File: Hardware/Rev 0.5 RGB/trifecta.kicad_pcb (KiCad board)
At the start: 2 copper layers, 361 x 120.8 mm, 286 parts, among them J1 USB2_C_Receptacle, J2 ISP Header, SW1 RESET, SW2 Rotary_Encoder_Switch, SW3 Rotary_Encoder_Switch, SW4 Rotary_Encoder_Switch, U1 ATmega32U4-AU, U2 SRV05-4, Y1 16MHz

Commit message: 8/8
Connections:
- J2 pad 5: RESET -> Net-(J2-Pad5)
- R1 pad 2: Net-(R1-Pad2) -> Net-(J2-Pad5)
- SW1 pad 2: Net-(R1-Pad2) -> Net-(J2-Pad5)
- U1 pad 13: Net-(R1-Pad2) -> Net-(J2-Pad5)
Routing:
- net Net-(R1-Pad2): track 38.4 -> 0.00 mm, vias 2 -> 0
- net Net-(J2-Pad5): track 0.00 -> 38.4 mm, vias 0 -> 2

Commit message: 8/8
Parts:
- J2: moved to B.Cu
- moved J2 3.52 mm to (157.5, -1.98), turned to 180 degrees
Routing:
- net row3: track 406.2 -> 458.6 mm, vias 7 -> 9
- net Net-(J2-Pad5): track 38.4 -> 90.5 mm, vias 2 -> 4
- net +5V: track 2351.0 -> 2382.4 mm, vias 90 -> 92
- net 0col: track 467.1 -> 491.4 mm
- net GND: track 2423.3 -> 2438.5 mm, vias 105 -> 107
- net col5: track 334.3 -> 349.4 mm, vias 1 -> 2
- added copper zone on B.Cu, net (none)
- added copper zone on F.Cu, net (none)

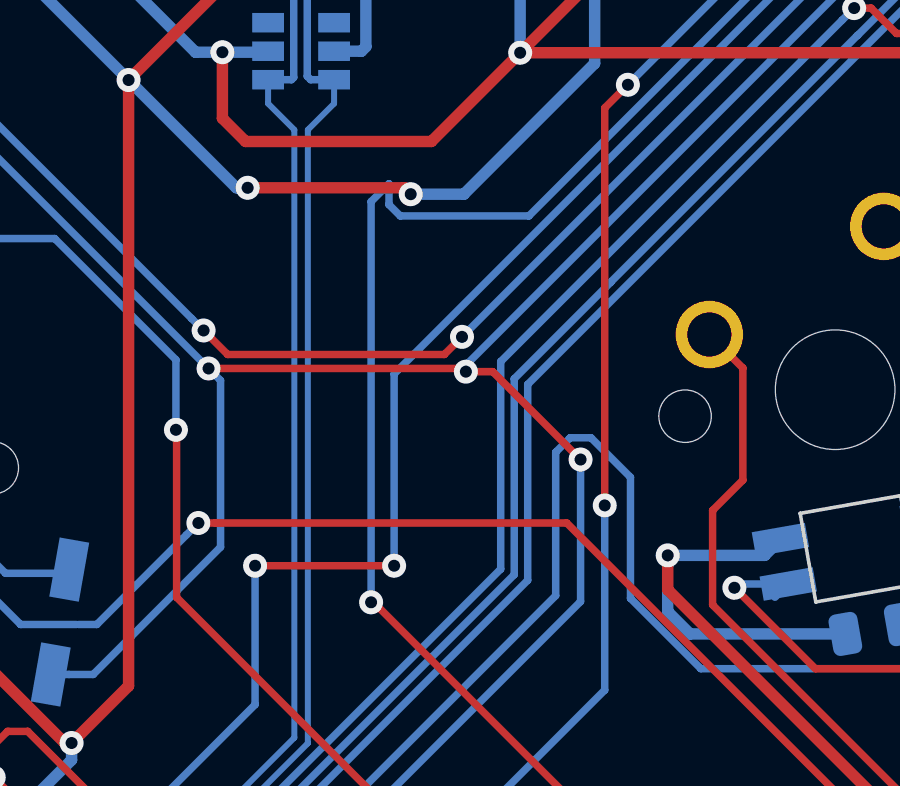
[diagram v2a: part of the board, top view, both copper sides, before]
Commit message: Clean up silkscreens, regenerate gerbers
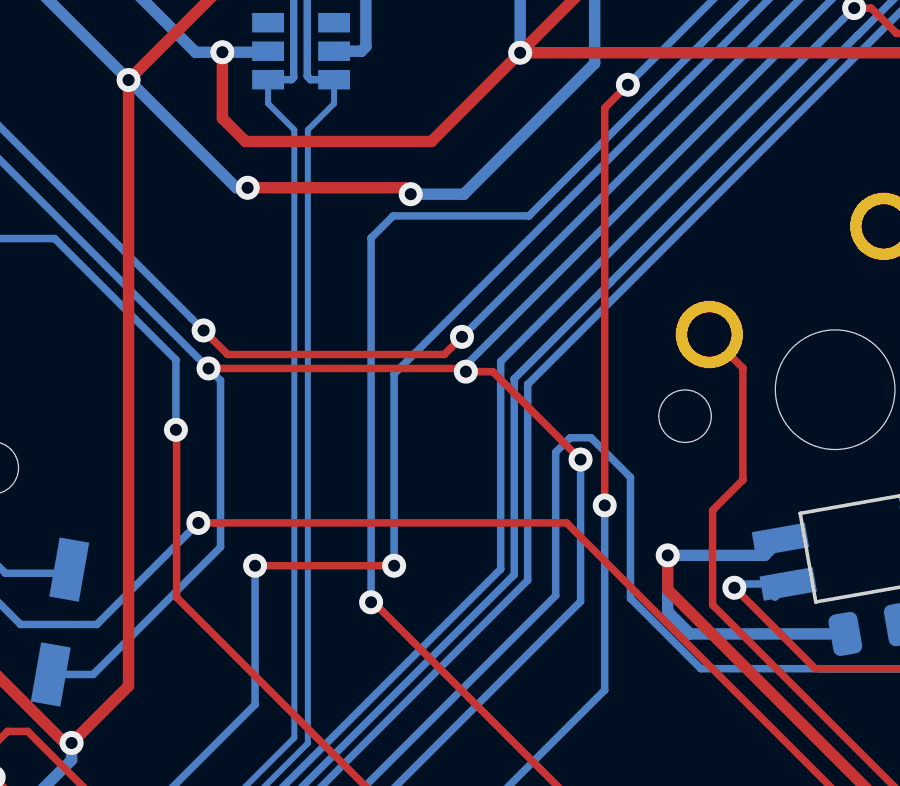
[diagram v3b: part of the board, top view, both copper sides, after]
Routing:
- net row3: track 458.6 -> 456.6 mm
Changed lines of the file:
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@@
-(kicad_pcb (version 20171130) (host pcbnew "(5.1.6)-1")
+(kicad_pcb (version 20171130) (host pcbnew "(5.1.4)-1")
   (general
     (thickness 1.6)
     (drawings 941)
-    (tracks 4406)
+    (tracks 4404)
     (zones 0)
     (modules 286)
@@
   (segment (start 152.25268 35.24504) (end 144.0688 27.06116) (width 0.25) (layer F.Cu) (net 10))
   (segment (start 144.0688 27.06116) (end 143.98244 27.06116) (width 0.25) (layer F.Cu) (net 10))
+  (segment (start 158.02356 0.5588) (end 157.46476 0.5588) (width 0.25) (layer B.Cu) (net 10))
+  (segment (start 143.98244 14.91756) (end 144.718079 14.181921) (width 0.25) (layer B.Cu) (net 10))
+  (segment (start 143.98244 27.06116) (end 143.98244 14.91756) (width 0.25) (layer B.Cu) (net 10))
+  (segment (start 144.718079 14.181921) (end 149.242801 14.181921) (width 0.25) (layer B.Cu) (net 10))
   (segment (start 149.242801 14.181921) (end 159.83712 3.587602) (width 0.25) (layer B.Cu) (net 10))
-  (segment (start 143.98244 13.704718) (end 144.578239 13.108919) (width 0.25) (layer B.Cu) (net 10))
-  (segment (start 144.955239 14.181921) (end 149.242801 14.181921) (width 0.25) (layer B.Cu) (net 10))
-  (segment (start 143.98244 27.06116) (end 143.98244 13.704718) (width 0.25) (layer B.Cu) (net 10))
-  (segment (start 144.578239 13.108919) (end 144.578239 13.804921) (width 0.25) (layer B.Cu) (net 10))
-  (segment (start 144.578239 13.804921) (end 144.955239 14.181921) (width 0.25) (layer B.Cu) (net 10))
   (segment (start 159.83712 3.587602) (end 159.83712 2.37236) (width 0.25) (layer B.Cu) (net 10))
-  (segment (start 158.02356 0.5588) (end 157.46476 0.5588) (width 0.25) (layer B.Cu) (net 10))
   (segment (start 159.83712 2.37236) (end 158.02356 0.5588) (width 0.25) (layer B.Cu) (net 10))
   (segment (start 170.469939 62.381213) (end 170.544767 62.381213) (width 0.25) (layer B.Cu) (net 11) (status 30))
